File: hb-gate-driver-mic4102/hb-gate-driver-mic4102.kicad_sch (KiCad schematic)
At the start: 12 parts

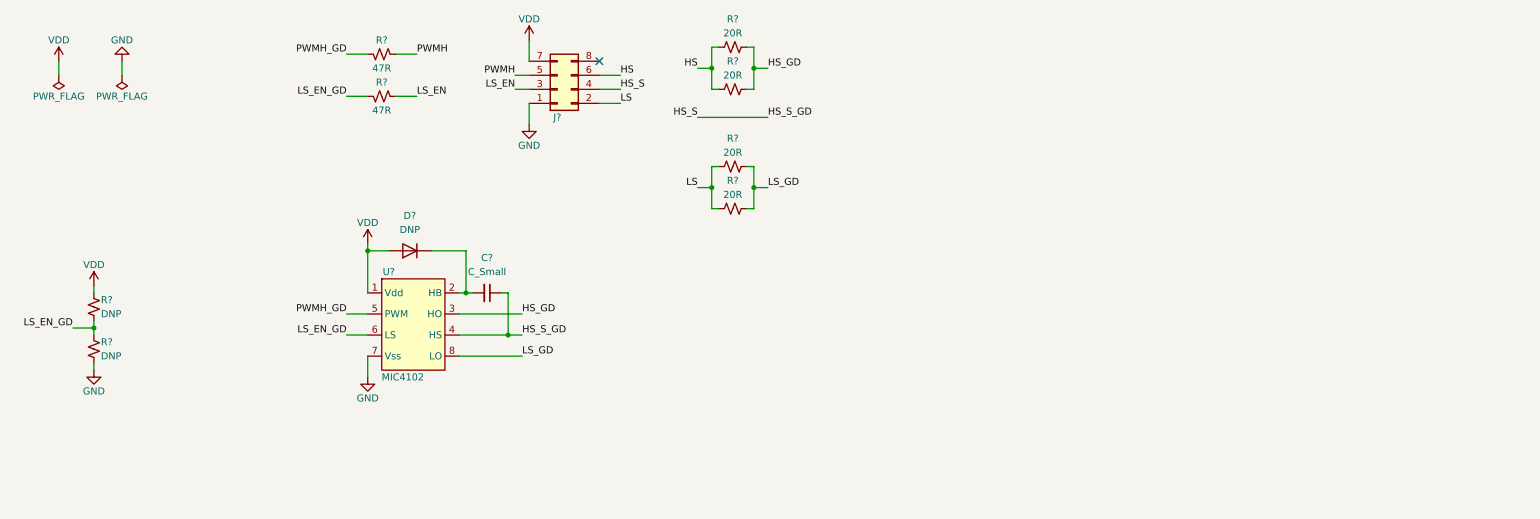
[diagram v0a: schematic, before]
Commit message: Schematics for MIC4102 gate driver
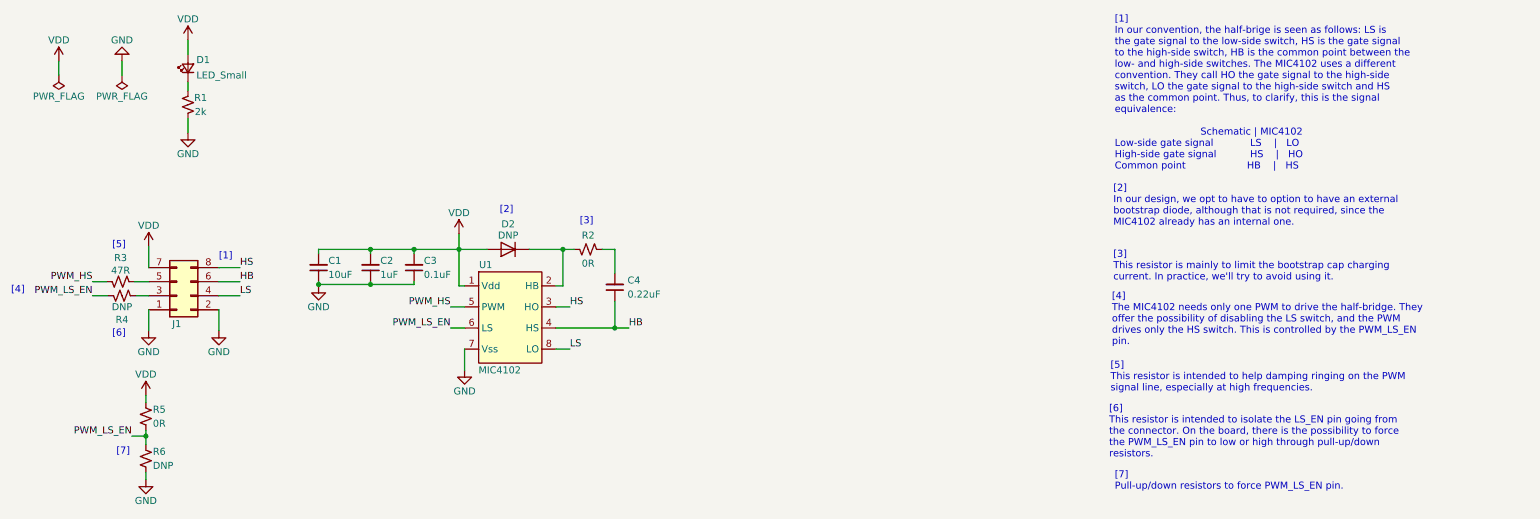
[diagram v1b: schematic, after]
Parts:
- removed R? (x4): 20R, Resistor_SMD:R_MELF_MMB-0207, symbol Device:R_Small_US
- removed R?: 47R, Resistor_SMD:R_0805_2012Metric_Pad1.20x1.40mm_HandSolder, symbol Device:R_Small_US
- added C1: 10uF, Capacitor_SMD:C_0805_2012Metric_Pad1.18x1.45mm_HandSolder, symbol Device:C_Small
- added C2: 1uF, Capacitor_SMD:C_0805_2012Metric_Pad1.18x1.45mm_HandSolder, symbol Device:C_Small
- added C3: 0.1uF, Capacitor_SMD:C_0805_2012Metric_Pad1.18x1.45mm_HandSolder, symbol Device:C_Small
- added D1: LED_Small, LED_SMD:LED_0805_2012Metric_Pad1.15x1.40mm_HandSolder, symbol Device:LED_Small
- added R1: 2k, Resistor_SMD:R_0805_2012Metric_Pad1.20x1.40mm_HandSolder, symbol Device:R_Small_US
- added R2: 0R, Resistor_SMD:R_0805_2012Metric_Pad1.20x1.40mm_HandSolder, symbol Device:R_Small_US
- added R4: DNP, Resistor_SMD:R_0805_2012Metric_Pad1.20x1.40mm_HandSolder, symbol Device:R_Small_US
- C4: renamed from C?; value C_Small -> 0.22uF
- R5: renamed from R?; value DNP -> 0R
- gave numbers to parts that had none: 5
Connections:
- net HS_GD is gone; now on net HS: U1.3 (HO)
- net LS_GD is gone; now on net LS: U1.8 (LO)
- net GND: now also J1.2 (Pin_2), C1.1, C2.1, C3.1, R1.1
- net HS: now also J1.8 (Pin_8); no longer J1.6 (Pin_6)
- net LS: now also J1.4 (Pin_4); no longer J1.2 (Pin_2)
- net VDD: now also C1.2, C2.2, C3.2, D1.2 (A)
- net at D2.1 (K), U1.2 (HB): now also R2.2; no longer C4.2
- net HS_S renamed HB
- net HB: now also J1.6 (Pin_6); no longer J1.4 (Pin_4)
- net LS_EN: no longer names the net of J1.3 (Pin_3)
- net LS_EN: now also R4.2
- net LS_EN_GD renamed PWM_LS_EN
- net PWM_LS_EN: now also R4.1
- net PWMH: no longer names the net of J1.5 (Pin_5), R3.1
- net PWMH_GD renamed PWM_HS
- new net: D1.1 (K), R1.2
- new net: C4.2, R2.1
- no-connect marks 1 -> 0
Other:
- note added: "[1]"
- note added: "[1] In our convention, the half-brige is seen as follows: LS is the gate signal to the low-side switch, HS is the gate signal to the high-side switch, HB is the common point between the low- and high-side switches. The MIC4102 uses a different convention. They call HO the gate signal to the high-side switch, LO the gate signal to the high-side switch and HS as the common point. Thus, to clarify, 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"
- note added: "[2]"
- note added: "[2] In our design, we opt to have to option to have an external bootstrap diode, although that is not required, since the MIC4102 already has an internal one."
- note added: "[3]"
- note added: "[3] This resistor is mainly to limit the bootstrap cap charging current. In practice, we'll try to avoid using it."
- note added: "[4]"
- note added: "[4] The MIC4102 needs only one PWM to drive the half-bridge. They offer the possibility of disabling the LS switch, and the PWM drives only the HS switch. This is controlled by the PWM_LS_EN pin."
- note added: "[5]"
- note added: "[5] This resistor is intended to help damping ringing on the PWM signal line, especially at high frequencies."
- note added: "[6]"
- note added: "[6] This resistor is intended to isolate the LS_EN pin going from the connector. On the board, there is the possibility to force the PWM_LS_EN pin to low or high through pull-up/down resistors."
- note added: "[7]"
- note added: "[7] Pull-up/down resistors to force PWM_LS_EN pin."
- moved on the sheet: C4, D2, J1, R3, R5, R6, U1

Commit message: Working on mic4102 schematics
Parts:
- C3: value 0.1uF -> 0.22uF
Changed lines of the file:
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@@
       (effects (font (size 1.27 1.27)) (justify right))
     )
-    (property "Value" "0.1uF" (id 1) (at 88.9 61.468 0)
+    (property "Value" "0.22uF" (id 1) (at 88.9 61.468 0)
       (effects (font (size 1.27 1.27)) (justify right))
     )
@@
     )
     (path "/d864a44e-cfd1-4618-9542-ec85cfd38a8e"
-      (reference "C3") (unit 1) (value "0.1uF") (footprint "Capacitor_SMD:C_0805_2012Metric_Pad1.18x1.45mm_HandSolder")
+      (reference "C3") (unit 1) (value "0.22uF") (footprint "Capacitor_SMD:C_0805_2012Metric_Pad1.18x1.45mm_HandSolder")
     )
     (path "/93427dec-2852-4ba5-be9a-39e01fe5acdf"
